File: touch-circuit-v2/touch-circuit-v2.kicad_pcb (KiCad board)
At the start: 2 copper layers, 18.7 x 20.5 mm, 12 parts, among them Q1 Q_PMOS_GSD, Q2 Q_NMOS_GSD

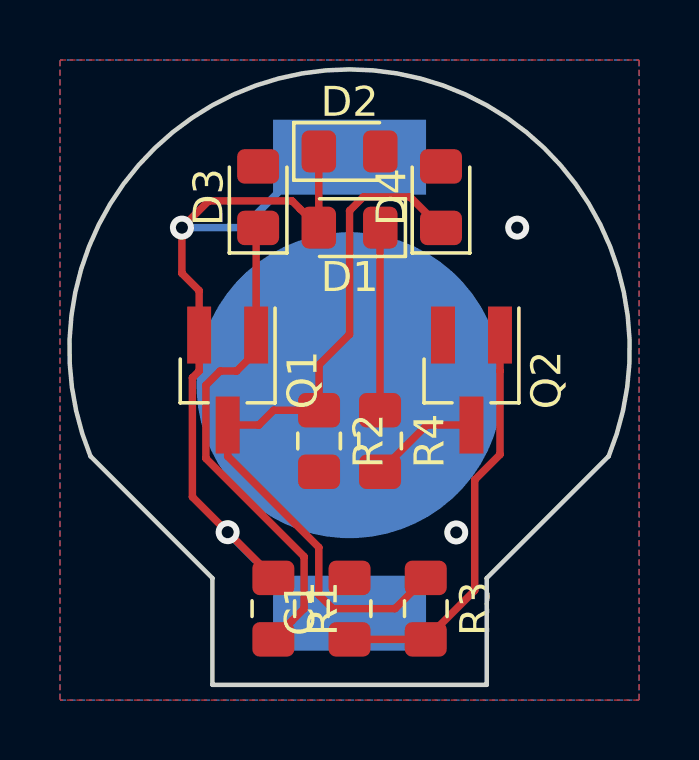
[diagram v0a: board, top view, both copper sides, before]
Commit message: reroute board
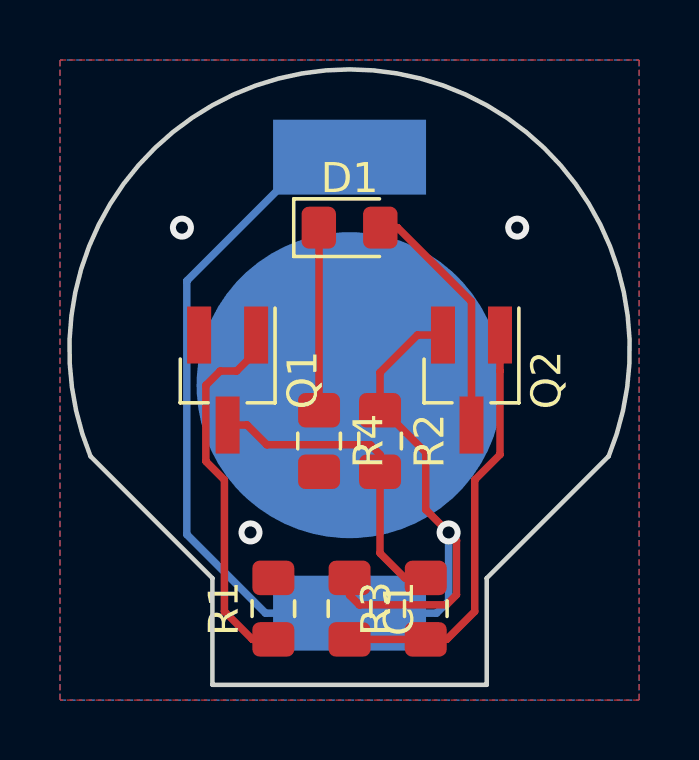
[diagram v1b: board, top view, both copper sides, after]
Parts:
- removed D2, D3, D4: D_Zener, Diode_SMD:D_0805_2012Metric_Pad1.15x1.40mm_HandSolder
- C1: value C -> 10uF
- Q1: value Q_PMOS_GSD -> Q_NMOS_GSD
- Q2: value Q_NMOS_GSD -> Q_PMOS_GSD
- R1: value R_US -> 3.3M
- R2: value R_US -> 56k
- R3: value R_US -> 82k
- R4: value R_US -> R_LED
- moved R2 2.03 mm to (143.3, 93.5)
- moved R4 2.03 mm to (141.2, 93.5)
- turned C1 to 270 degrees
- turned D1 to 0 degrees
- turned R1 to 90 degrees
- turned R3 to 90 degrees
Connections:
- C1 pad 1: Net-(C1-Pad1) -> Net-(BT1-Pad1)
- C1 pad 2: GND -> Net-(C1-Pad2)
- D1 pad 2: Net-(BT1-Pad1) -> Net-(D1-Pad2)
- Q1 pad 1: Net-(D3-Pad1) -> /Gate
- Q1 pad 2: Net-(BT1-Pad1) -> GND
- Q1 pad 3: Net-(D4-Pad1) -> Net-(Q1-Pad3)
- Q2 pad 1: Net-(C1-Pad1) -> Net-(C1-Pad2)
- Q2 pad 2: GND -> Net-(BT1-Pad1)
- Q2 pad 3: Net-(Q2-Pad3) -> Net-(D1-Pad2)
- R1 pad 1: Net-(BT1-Pad1) -> /Gate
- R1 pad 2: Net-(D3-Pad1) -> GND
- R2 pad 1: Net-(D4-Pad1) -> Net-(BT1-Pad1)
- R2 pad 2: GND -> Net-(Q1-Pad3)
- R3 pad 1: Net-(D4-Pad1) -> Net-(C1-Pad2)
- R3 pad 2: Net-(C1-Pad1) -> Net-(Q1-Pad3)
- R4 pad 2: Net-(Q2-Pad3) -> GND
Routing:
- net Net-(D4-Pad1): track 25.1 -> 0.00 mm
- net Net-(D3-Pad1): track 16.5 -> 0.00 mm
- net Net-(C1-Pad2): track 0.00 -> 14.1 mm
- net Net-(C1-Pad1): track 13.7 -> 0.00 mm
- net /Gate: track 0.00 -> 12.5 mm
- net Net-(BT1-Pad1): track 32.7 -> 43.4 mm, vias 2 -> 1
- net Net-(Q1-Pad3): track 0.00 -> 10.6 mm
- net Net-(D1-Pad2): track 0.00 -> 8.18 mm
- net Net-(Q2-Pad3): track 3.69 -> 0.00 mm
- net GND: vias 2 -> 3

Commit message: add the mounting holes and clean up the fab layer
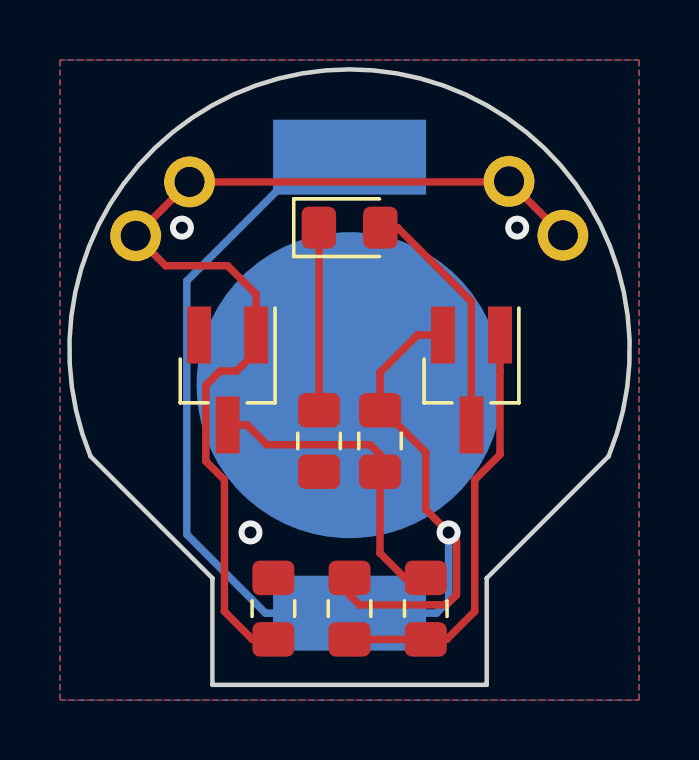
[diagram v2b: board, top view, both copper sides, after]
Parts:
- added REF**: WireMount, #footprints:WireMount, F.Cu at (136.9, 84.8)
- added REF**: WireMount, #footprints:WireMount, F.Cu at (147.6, 84.8)
- Q1: value Q_NMOS_GSD -> NMOS
- Q2: value Q_PMOS_GSD -> PMOS
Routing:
- net /Gate: track 12.5 -> 34.4 mm
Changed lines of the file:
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@@
     (thickness 1.6)
     (drawings 6)
-    (tracks 54)
+    (tracks 64)
     (zones 0)
-    (modules 9)
+    (modules 11)
     (nets 8)
   )
@@
     (0 F.Cu signal)
     (31 B.Cu signal)
-    (32 B.Adhes user)
-    (33 F.Adhes user)
+    (32 B.Adhes user hide)
+    (33 F.Adhes user hide)
     (34 B.Paste user hide)
-    (35 F.Paste user)
-    (36 B.SilkS user hide)
-    (37 F.SilkS user hide)
-    (38 B.Mask user hide)
+    (35 F.Paste user hide)
+    (36 B.SilkS user)
+    (37 F.SilkS user)
+    (38 B.Mask user)
     (39 F.Mask user)
-    (40 Dwgs.User user)
-    (41 Cmts.User user)
-    (42 Eco1.User user)
-    (43 Eco2.User user)
+    (40 Dwgs.User user hide)
+    (41 Cmts.User user hide)
+    (42 Eco1.User user hide)
+    (43 Eco2.User user hide)
     (44 Edge.Cuts user)
-    (45 Margin user)
+    (45 Margin user hide)
     (46 B.CrtYd user)
     (47 F.CrtYd user)
-    (48 B.Fab user hide)
-    (49 F.Fab user hide)
+    (48 B.Fab user)
+    (49 F.Fab user)
   )
   (setup
@@
     (mod_text_size 1 1)
     (mod_text_width 0.15)
-    (pad_size 1.524 1.524)
-    (pad_drill 0.762)
+    (pad_size 1.7 1.7)
+    (pad_drill 1)
     (pad_to_mask_clearance 0.051)
     (solder_mask_min_width 0.25)
@@
     (add_net "Net-(Q1-Pad3)")
   )
+  (module "#footprints:WireMount" (layer F.Cu)
+    (at 136.906 84.836 315)
+    (descr "Through hole straight pin header, 1x02, 2.54mm pitch, single row")
+    (tags "Through hole pin header THT 1x02 2.54mm single row")
+    (fp_text reference REF** (at 0 -2.33 135) (layer F.SilkS) hide
+      (effects (font (size 1 1) (thickness 0.15)))
+    )
+    (fp_text value WireMount (at -1.616446 -1.616446) (layer F.Fab)
+      (effects (font (size 1 1) (thickness 0.15)))
+    )
+    (fp_line (start -1 -1) (end 1 -1) (layer F.Fab) (width 0.1))
+    (fp_line (start 1 -1) (end 1 3.5) (layer F.Fab) (width 0.1))
+    (fp_line (start 1 3.5) (end -1 3.5) (layer F.Fab) (width 0.1))
+    (fp_line (start -1 3.5) (end -1 -1) (layer F.Fab) (width 0.1))
+    (fp_line (start -1 -1) (end -1 3.5) (layer F.CrtYd) (width 0.05))
+    (fp_line (start -1 3.5) (end 1 3.5) (layer F.CrtYd) (width 0.05))
+    (fp_line (start 1 3.5) (end 1 -1) (layer F.CrtYd) (width 0.05))
+    (fp_line (start 1 -1) (end -1 -1) (layer F.CrtYd) (width 0.05))
+    (fp_text user %R (at 0 1.270001 45) (layer F.Fab) hide
+      (effects (font (size 1 1) (thickness 0.15)))
+    )
+    (pad 1 thru_hole circle (at 0 0 315) (size 1.7 1.7) (drill 1) (layers *.Cu *.Mask)
+      (net 7 /Gate))
+    (pad 2 thru_hole oval (at 0 2.54 315) (size 1.7 1.7) (drill 1) (layers *.Cu *.Mask)
+      (net 7 /Gate))
+    (model ${KISYS3DMOD}/Connector_PinHeader_2.54mm.3dshapes/PinHeader_1x02_P2.54mm_Vertical.wrl
+      (at (xyz 0 0 0))
+      (scale (xyz 1 1 1))
+      (rotate (xyz 0 0 0))
+    )
+  )
+  (module "#footprints:WireMount" (layer F.Cu)
+    (at 147.555949 84.817949 45)
+    (descr "Through hole straight pin header, 1x02, 2.54mm pitch, single row")
+    (tags "Through hole pin header THT 1x02 2.54mm single row")
+    (fp_text reference REF** (at 0 -2.33 45) (layer F.SilkS) hide
+      (effects (font (size 1 1) (thickness 0.15)))
+    )
+    (fp_text value WireMount (at 1.616446 -1.590918) (layer F.Fab)
+      (effects (font (size 1 1) (thickness 0.15)))
+    )
+    (fp_text user %R (at 0 1.270001 135) (layer F.Fab) hide
+      (effects (font (size 1 1) (thickness 0.15)))
+    )
+    (fp_line (start 1 -1) (end -1 -1) (layer F.CrtYd) (width 0.05))
+    (fp_line (start 1 3.5) (end 1 -1) (layer F.CrtYd) (width 0.05))
+    (fp_line (start -1 3.5) (end 1 3.5) (layer F.CrtYd) (width 0.05))
+    (fp_line (start -1 -1) (end -1 3.5) (layer F.CrtYd) (width 0.05))
+    (fp_line (start -1 3.5) (end -1 -1) (layer F.Fab) (width 0.1))
+    (fp_line (start 1 3.5) (end -1 3.5) (layer F.Fab) (width 0.1))
+    (fp_line (start 1 -1) (end 1 3.5) (layer F.Fab) (width 0.1))
+    (fp_line (start -1 -1) (end 1 -1) (layer F.Fab) (width 0.1))
+    (pad 2 thru_hole oval (at 0 2.54 45) (size 1.7 1.7) (drill 1) (layers *.Cu *.Mask)
+      (net 7 /Gate))
+    (pad 1 thru_hole circle (at 0 0 45) (size 1.7 1.7) (drill 1) (layers *.Cu *.Mask)
+      (net 7 /Gate))
+    (model ${KISYS3DMOD}/Connector_PinHeader_2.54mm.3dshapes/PinHeader_1x02_P2.54mm_Vertical.wrl
+      (at (xyz 0 0 0))
+      (scale (xyz 1 1 1))
+      (rotate (xyz 0 0 0))
+    )
+  )
   (module Battery:BatteryHolder_LINX_BAT-HLD-012-SMT (layer B.Cu)
     (at 142.24 91.611001 90)
@@
     (tags "battery holder coin cell cr1216 cr1220 cr1225")
     (attr smd)
-    (fp_text reference BT1 (at 0 -6 90) (layer B.SilkS)
+    (fp_text reference BT1 (at 0 -6 90) (layer B.SilkS) hide
       (effects (font (size 1 1) (thickness 0.15)) (justify mirror))
     )
-    (fp_text value Battery_Cell (at 0 7 90) (layer B.Fab)
+    (fp_text value Battery_Cell (at 8.807001 0 180) (layer B.Fab)
       (effects (font (size 1 1) (thickness 0.15)) (justify mirror))
     )
@@
     (tags "capacitor handsolder")
     (attr smd)
-    (fp_text reference C1 (at 0 -1.65 90) (layer F.SilkS)
-      (effects (font (size 1 1) (thickness 0.15)))
-    )
-    (fp_text value 10uF (at 0 1.65 90) (layer F.Fab)
+    (fp_text reference C1 (at 0 -1.65 90) (layer F.SilkS) hide
+      (effects (font (size 1 1) (thickness 0.15)))
+    )
+    (fp_text value 10uF (at 2.032 0 180) (layer F.Fab)
       (effects (font (size 1 1) (thickness 0.15)))
     )
@@
     (tags "LED handsolder")
     (attr smd)
-    (fp_text reference D1 (at 0 -1.65 180) (layer F.SilkS)
+    (fp_text reference D1 (at 0 -1.65 180) (layer F.SilkS) hide
       (effects (font (size 1 1) (thickness 0.15)))
     )
@@
     (tags SOT-23)
     (attr smd)
-    (fp_text reference Q1 (at 0 -2.5 270) (layer F.SilkS)
-      (effects (font (size 1 1) (thickness 0.15)))
-    )
-    (fp_text value Q_NMOS_GSD (at 0 2.5 270) (layer F.Fab)
+    (fp_text reference Q1 (at 0 -2.5 270) (layer F.SilkS) hide
+      (effects (font (size 1 1) (thickness 0.15)))
+    )
+    (fp_text value NMOS (at -1.524 0) (layer F.Fab)
       (effects (font (size 1 1) (thickness 0.15)))
     )
@@
     (tags SOT-23)
     (attr smd)
-    (fp_text reference Q2 (at 0 -2.5 270) (layer F.SilkS)
-      (effects (font (size 1 1) (thickness 0.15)))
-    )
-    (fp_text value Q_PMOS_GSD (at 0 2.5 270) (layer F.Fab)
+    (fp_text reference Q2 (at 0 -2.5 270) (layer F.SilkS) hide
+      (effects (font (size 1 1) (thickness 0.15)))
+    )
+    (fp_text value PMOS (at -1.524 0) (layer F.Fab)
       (effects (font (size 1 1) (thickness 0.15)))
     )
@@
     (tags "resistor handsolder")
     (attr smd)
-    (fp_text reference R1 (at 0 -1.65 270) (layer F.SilkS)
-      (effects (font (size 1 1) (thickness 0.15)))
-    )
-    (fp_text value 3.3M (at 0 1.65 270) (layer F.Fab)
+    (fp_text reference R1 (at 0 -1.65 270) (layer F.SilkS) hide
+      (effects (font (size 1 1) (thickness 0.15)))
+    )
+    (fp_text value 3.3M (at 0 -2.794) (layer F.Fab)
       (effects (font (size 1 1) (thickness 0.15)))
     )
@@
     (tags "resistor handsolder")
     (attr smd)
-    (fp_text reference R2 (at 0 -1.65 270) (layer F.SilkS)
-      (effects (font (size 1 1) (thickness 0.15)))
-    )
-    (fp_text value 56k (at 0 1.65 270) (layer F.Fab)
+    (fp_text reference R2 (at 0 -1.65 270) (layer F.SilkS) hide
+      (effects (font (size 1 1) (thickness 0.15)))
+    )
+    (fp_text value 56k (at 0 -2.286) (layer F.Fab)
       (effects (font (size 1 1) (thickness 0.15)))
     )
@@
     (tags "resistor handsolder")
     (attr smd)
-    (fp_text reference R3 (at 0 -1.65 270) (layer F.SilkS)
-      (effects (font (size 1 1) (thickness 0.15)))
-    )
-    (fp_text value 82k (at 0 1.65 270) (layer F.Fab)
+    (fp_text reference R3 (at 0 -1.65 270) (layer F.SilkS) hide
+      (effects (font (size 1 1) (thickness 0.15)))
+    )
+    (fp_text value 82k (at 0 2.286) (layer F.Fab)
       (effects (font (size 1 1) (thickness 0.15)))
     )
@@
     (tags "resistor handsolder")
     (attr smd)
-    (fp_text reference R4 (at 0 -1.65 270) (layer F.SilkS)
-      (effects (font (size 1 1) (thickness 0.15)))
-    )
-    (fp_text value R_LED (at 0 1.65 270) (layer F.Fab)
+    (fp_text reference R4 (at 0 -1.65 270) (layer F.SilkS) hide
+      (effects (font (size 1 1) (thickness 0.15)))
+    )
+    (fp_text value R_LED (at 0 3.175) (layer F.Fab)
       (effects (font (size 1 1) (thickness 0.15)))
     )
@@
   (segment (start 139 100.085) (end 138.06801 99.15301) (width 0.25) (layer F.Cu) (net 7))
   (segment (start 139.7 100.085) (end 139 100.085) (width 0.25) (layer F.Cu) (net 7))
+  (segment (start 136.056001 85.685999) (end 135.109949 86.632051) (width 0.25) (layer F.Cu) (net 7))
+  (segment (start 136.906 84.836) (end 136.056001 85.685999) (width 0.25) (layer F.Cu) (net 7))
+  (segment (start 148.405948 85.667948) (end 149.352 86.614) (width 0.25) (layer F.Cu) (net 7))
+  (segment (start 147.555949 84.817949) (end 148.405948 85.667948) (width 0.25) (layer F.Cu) (net 7))
+  (segment (start 147.537898 84.836) (end 147.555949 84.817949) (width 0.25) (layer F.Cu) (net 7))
+  (segment (start 136.906 84.836) (end 147.537898 84.836) (width 0.25) (layer F.Cu) (net 7))
+  (segment (start 139.126 88.58) (end 139.126 89.94) (width 0.25) (layer F.Cu) (net 7))
+  (segment (start 138.176 87.63) (end 139.126 88.58) (width 0.25) (layer F.Cu) (net 7))
+  (segment (start 136.107898 87.63) (end 138.176 87.63) (width 0.25) (layer F.Cu) (net 7))
+  (segment (start 135.109949 86.632051) (end 136.107898 87.63) (width 0.25) (layer F.Cu) (net 7))
   (zone (net 2) (net_name GND) (layer F.Cu) (hatch edge 0.508)
     (connect_pads (clearance 0.508))
